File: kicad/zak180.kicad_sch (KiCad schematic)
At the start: 10 parts, among them U11 74HC02, U16 74HC00

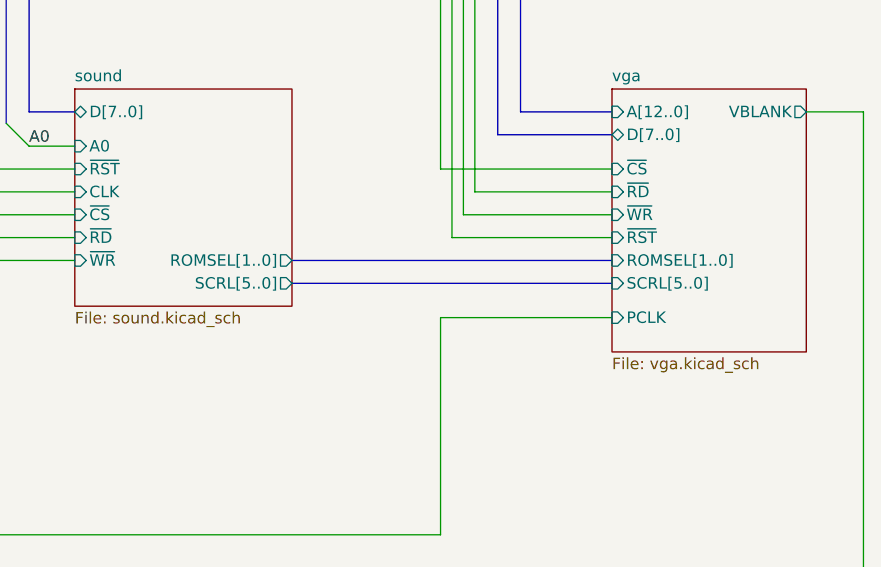
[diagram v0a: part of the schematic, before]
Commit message: hw: color text mode VGA (WIP)
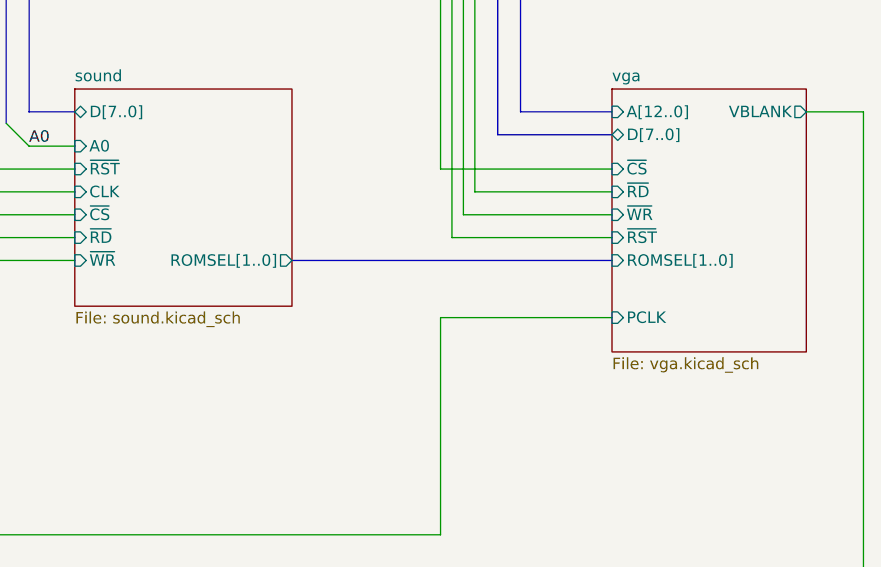
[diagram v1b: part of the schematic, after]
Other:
- sheet sound ports: added none; removed SCRL[5..0]
- sheet vga ports: added none; removed SCRL[5..0]
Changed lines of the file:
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@@
-		)
-	)
-	(bus
-		(pts
-			(xy 207.01 130.81) (xy 242.57 130.81)
-		)
-		(stroke
-			(width 0)
-			(type default)
 		)
 	)
@@
 			)
 		)
-		(pin "SCRL[5..0]" output
-			(at 207.01 130.81 0)
-			(effects
-				(font
-					(size 1.27 1.27)
-				)
-				(justify right)
-			)
-		)
 		(pin "ROMSEL[1..0]" output
 			(at 207.01 128.27 0)
@@
 			(effects
 				(font
-					(size 1.27 1.27)
-				)
-				(justify left)
-			)
-		)
-		(pin "SCRL[5..0]" input
-			(at 242.57 130.81 180)
-			(effects
-				(font
